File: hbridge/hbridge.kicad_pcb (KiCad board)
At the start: 2 copper layers, 212.8 x 102.7 mm, 23 parts, among them J1 From_MCU, J10 From_MCU, J11 MOSFET_out, J12 Conn_01x03, J13 Conn_01x01_Socket, J14 Conn_01x01_Socket, J19 24V, J2 MOSFET_out, J21 Conn_01x01_Socket, J3 Conn_01x03, J4 From_MCU, J5 MOSFET_out, J6 Conn_01x03, J7 From_MCU, J8 MOSFET_out, J9 Conn_01x03, U1 LDO-3.3, U20 B2412S-2WR3, U4 AM6TW-2415DZ, U9 AM6TW-2415DZ

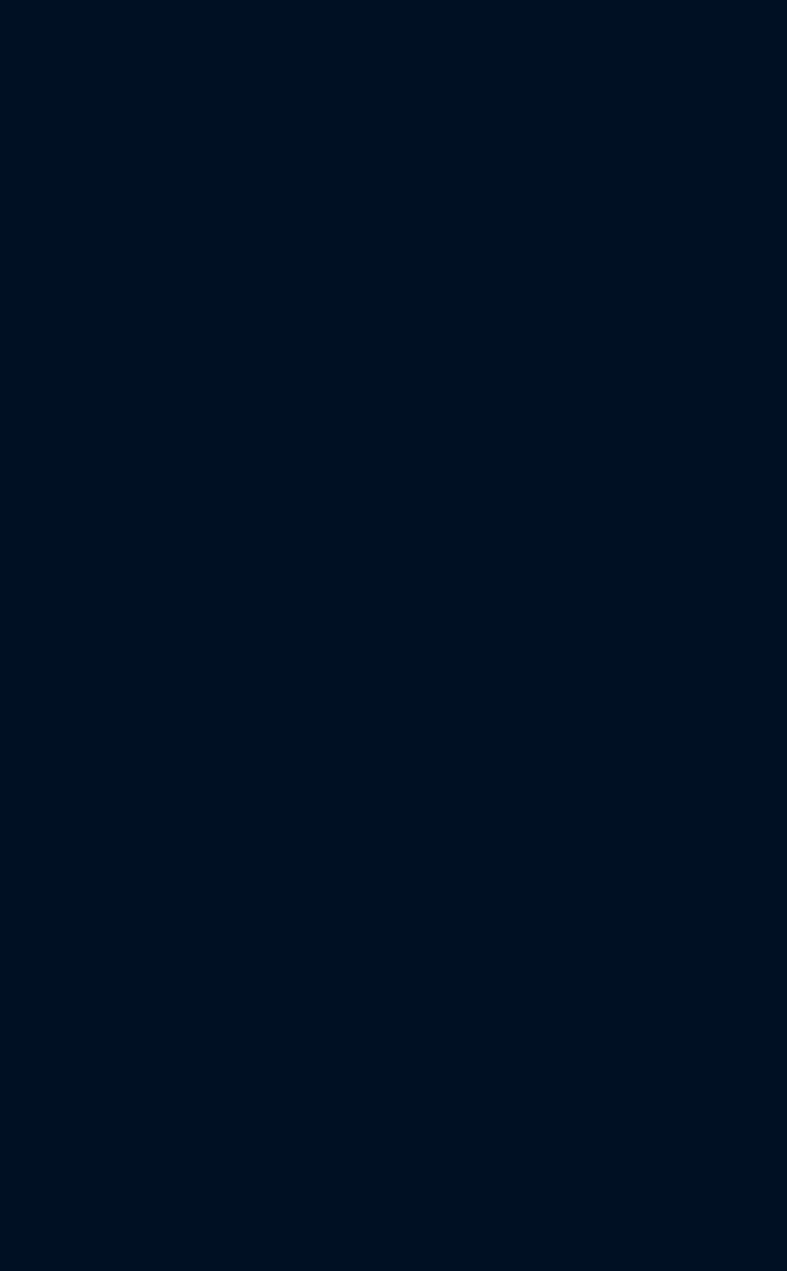
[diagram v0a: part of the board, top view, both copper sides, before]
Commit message: Half-bridge refactoring start.
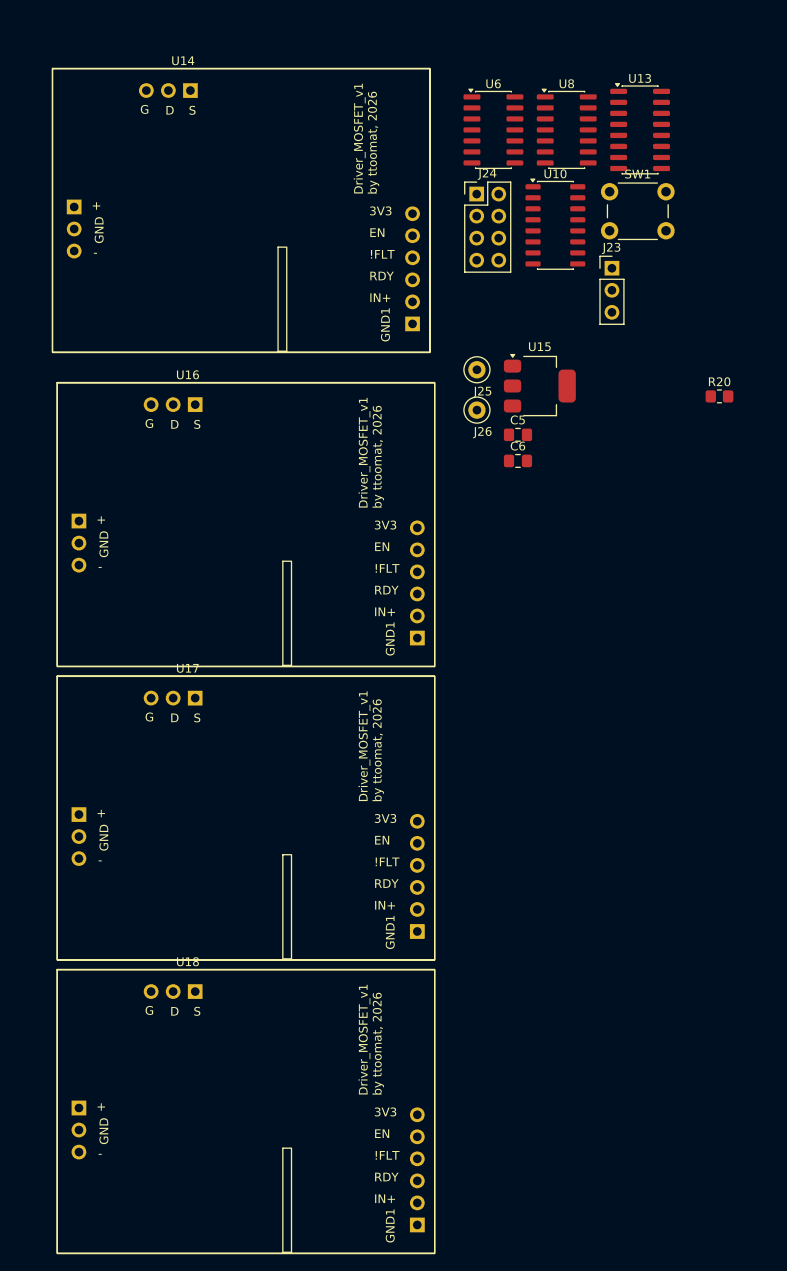
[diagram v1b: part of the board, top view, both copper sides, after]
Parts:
- added C5: 10u, Capacitor_SMD:C_0805_2012Metric_Pad1.18x1.45mm_HandSolder, F.Cu at (186.2, 387.9)
- added C6: 2.2u, Capacitor_SMD:C_0805_2012Metric_Pad1.18x1.45mm_HandSolder, F.Cu at (186.2, 390.9)
- added J23: Conn_01x03, Connector_PinHeader_2.54mm:PinHeader_1x03_P2.54mm_Vertical, F.Cu at (197.0, 368.7)
- added J24: Conn_01x08_Pin, Connector_PinHeader_2.54mm:PinHeader_2x04_P2.54mm_Vertical, F.Cu at (181.4, 360.2)
- added J25: Conn_01x01_Socket, TestPoint:TestPoint_Loop_D1.80mm_Drill1.0mm_Beaded, F.Cu at (181.4, 380.4)
- added J26: Conn_01x01_Socket, TestPoint:TestPoint_Loop_D1.80mm_Drill1.0mm_Beaded, F.Cu at (181.4, 385.1)
- added R20: 1k, Resistor_SMD:R_0805_2012Metric_Pad1.20x1.40mm_HandSolder, F.Cu at (209.4, 383.5)
- added SW1: SW_Push, Button_Switch_THT:SW_PUSH_6mm_H4.3mm, F.Cu at (196.7, 359.9)
- added U10: 74HC165, Package_SO:SO-16_3.9x9.9mm_P1.27mm, F.Cu at (190.5, 363.8)
- added U13: CD4043B, Package_SO:SOIC-16_3.9x9.9mm_P1.27mm, F.Cu at (200.2, 352.8)
- added U14: driver_MOSFET_board, Tamara:плата драйвера, F.Cu at (154.2, 362.0)
- added U15: LDO-3.3, Package_TO_SOT_SMD:SOT-223-3_TabPin2, F.Cu at (188.7, 382.3)
- added U16: driver_MOSFET_board, Tamara:плата драйвера, F.Cu at (154.8, 398.2)
- added U17: driver_MOSFET_board, Tamara:плата драйвера, F.Cu at (154.8, 432.1)
- added U18: driver_MOSFET_board, Tamara:плата драйвера, F.Cu at (154.8, 465.9)
- added U6: MC74HC08ADG (74HC08), Package_SO:SOIC-14_3.9x8.7mm_P1.27mm, F.Cu at (183.3, 352.8)
- added U8: 74AHC04, Package_SO:SOIC-14_3.9x8.7mm_P1.27mm, F.Cu at (191.8, 352.8)
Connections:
- net /драйверы/drain1 renamed /драйверы old/drain1
- net /драйверы/drain2 renamed /драйверы old/drain2
- net /драйверы/drain4 renamed /драйверы old/drain4
- net /драйверы/gate1 renamed /драйверы old/gate1
- net /драйверы/gate2 renamed /драйверы old/gate2
- net /драйверы/gate3 renamed /драйверы old/gate3
- net /драйверы/gate4 renamed /драйверы old/gate4
